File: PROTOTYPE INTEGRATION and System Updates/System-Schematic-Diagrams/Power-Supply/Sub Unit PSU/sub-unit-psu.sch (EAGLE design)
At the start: 8 parts, among them U1 BA033CC0FP-E2TO252-3_ROM, U3 L7805CV

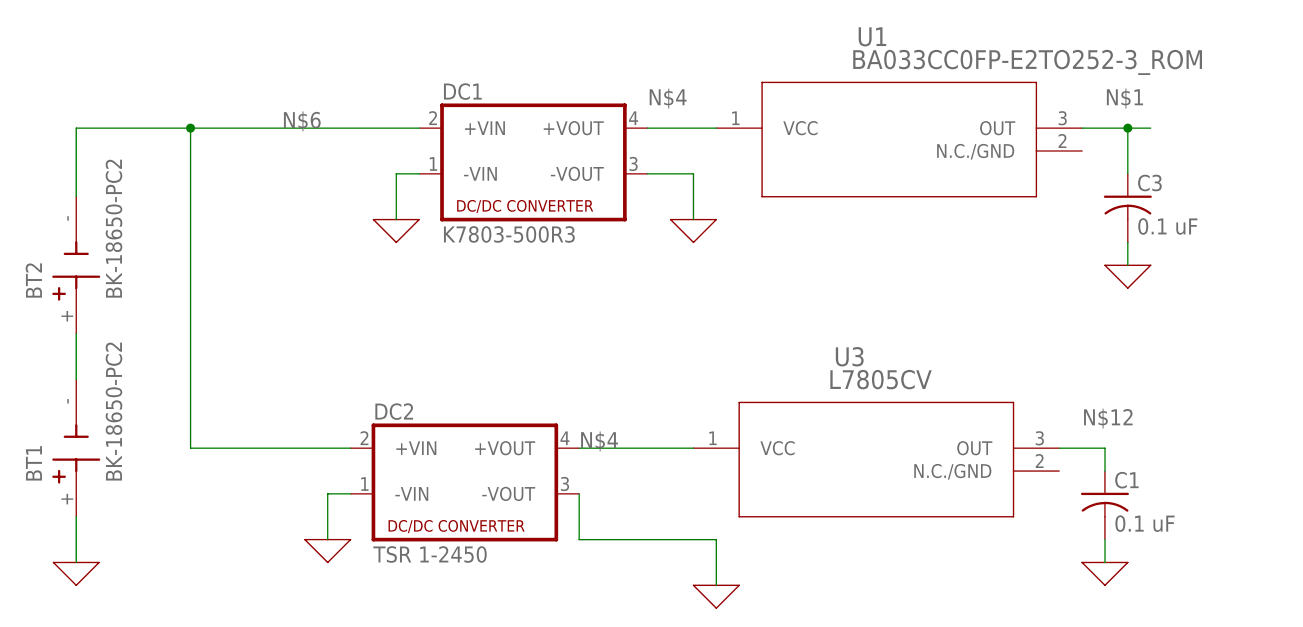
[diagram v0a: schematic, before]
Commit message: Updated Individual schematics, bd and pictures
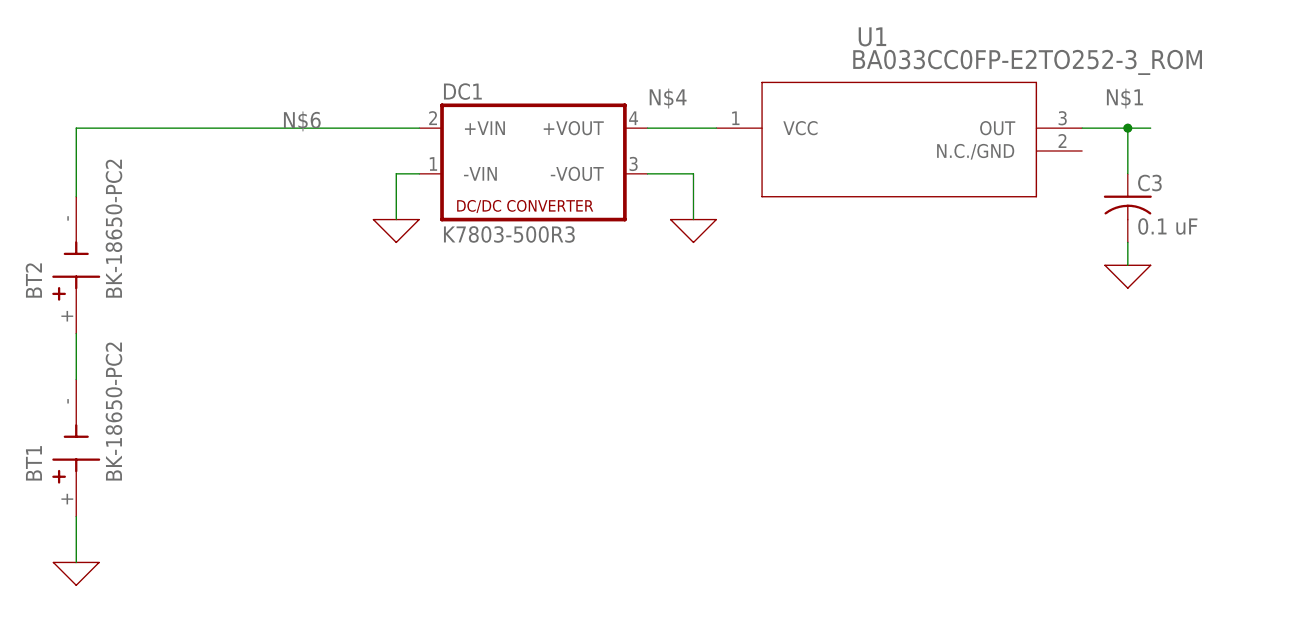
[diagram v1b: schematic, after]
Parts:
- removed C1: 0.1 uF, rcl:C-US050-024X044
- removed DC2: TSR 1-2450, dc-dc-converter:NME
- removed U3: L7805CV, 2023-03-08_12-17-23_Library:BA033CC0FP-E2TO252-3_ROM
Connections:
- removed net N$12: C1.1, U3.OUT
- net 0: no longer C1.2, DC2.-VIN, DC2.-VOUT
- net N$4: no longer DC2.+VOUT, U3.VCC
- net N$6: no longer DC2.+VIN
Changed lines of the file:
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@@
 <part name="C3" library="rcl" library_urn="urn:adsk.eagle:library:334" deviceset="C-US" device="050-024X044" package3d_urn="urn:adsk.eagle:package:23643/1" value="0.1 uF"/>
 <part name="X_10" library="ngspice-simulation" library_urn="urn:adsk.eagle:library:527439" deviceset="GND" device=""/>
-<part name="DC2" library="dc-dc-converter" library_urn="urn:adsk.eagle:library:208" deviceset="NME" device="" package3d_urn="urn:adsk.eagle:package:12313/1" value="TSR 1-2450"/>
-<part name="X_6" library="ngspice-simulation" library_urn="urn:adsk.eagle:library:527439" deviceset="GND" device=""/>
-<part name="U3" library="2023-03-08_12-17-23_Library" deviceset="BA033CC0FP-E2" device="TO252-3_ROM" value="L7805CV"/>
-<part name="X_8" library="ngspice-simulation" library_urn="urn:adsk.eagle:library:527439" deviceset="GND" device=""/>
-<part name="C1" library="rcl" library_urn="urn:adsk.eagle:library:334" deviceset="C-US" device="050-024X044" package3d_urn="urn:adsk.eagle:package:23643/1" value="0.1 uF"/>
-<part name="X_3" library="ngspice-simulation" library_urn="urn:adsk.eagle:library:527439" deviceset="GND" device=""/>
 </parts>
 <sheets>
@@
 </instance>
 <instance part="X_10" gate="G$1" x="233.68" y="134.62" smashed="yes"/>
-<instance part="DC2" gate="G$1" x="160.02" y="111.76" smashed="yes">
-<attribute name="NAME" x="149.86" y="117.475" size="1.778" layer="95"/>
-<attribute name="VALUE" x="149.86" y="101.6" size="1.778" layer="96"/>
-</instance>
-<instance part="X_6" gate="G$1" x="144.78" y="104.14" smashed="yes"/>
-<instance part="U3" gate="A" x="182.88" y="114.3" smashed="yes">
-<attribute name="NAME" x="201.0146" y="123.4186" size="2.083" layer="95" ratio="6"/>
-<attribute name="VALUE" x="200.3752" y="120.8786" size="2.083" layer="96" ratio="6"/>
-</instance>
-<instance part="X_8" gate="G$1" x="187.96" y="99.06" smashed="yes"/>
-<instance part="C1" gate="G$1" x="231.14" y="109.22" smashed="yes">
-<attribute name="NAME" x="232.156" y="109.855" size="1.778" layer="95"/>
-<attribute name="VALUE" x="232.156" y="105.029" size="1.778" layer="96"/>
-</instance>
-<instance part="X_3" gate="G$1" x="231.14" y="101.6" smashed="yes"/>
 </instances>
 <busses>
@@
 <wire x1="233.68" y1="134.62" x2="233.68" y2="137.16" width="0.1524" layer="91"/>
 </segment>
-<segment>
-<pinref part="X_6" gate="G$1" pin="0"/>
-<pinref part="DC2" gate="G$1" pin="-VIN"/>
-<wire x1="144.78" y1="104.14" x2="144.78" y2="109.22" width="0.1524" layer="91"/>
-<wire x1="144.78" y1="109.22" x2="147.32" y2="109.22" width="0.1524" layer="91"/>
-</segment>
-<segment>
-<pinref part="DC2" gate="G$1" pin="-VOUT"/>
-<wire x1="172.72" y1="109.22" x2="172.72" y2="104.14" width="0.1524" layer="91"/>
-<wire x1="172.72" y1="104.14" x2="187.96" y2="104.14" width="0.1524" layer="91"/>
-<pinref part="X_8" gate="G$1" pin="0"/>
-<wire x1="187.96" y1="99.06" x2="187.96" y2="104.14" width="0.1524" layer="91"/>
-</segment>
-<segment>
-<pinref part="X_3" gate="G$1" pin="0"/>
-<pinref part="C1" gate="G$1" pin="2"/>
-<wire x1="231.14" y1="101.6" x2="231.14" y2="104.14" width="0.1524" layer="91"/>
-</segment>
 </net>
 <net name="N$4" class="0">
@@
 <label x="180.34" y="152.4" size="1.778" layer="95"/>
 <pinref part="U1" gate="A" pin="VCC"/>
-</segment>
-<segment>
-<pinref part="DC2" gate="G$1" pin="+VOUT"/>
-<wire x1="172.72" y1="114.3" x2="185.42" y2="114.3" width="0.1524" layer="91"/>
-<label x="172.72" y="114.3" size="1.778" layer="95"/>
-<pinref part="U3" gate="A" pin="VCC"/>
 </segment>
 </net>
@@
 </segment>
 </net>
-<net name="N$12" class="0">
+<net name="N$6" class="0">
 <segment>
-<wire x1="226.06" y1="114.3" x2="231.14" y2="114.3" width="0.1524" layer="91"/>
-<label x="228.6" y="116.84" size="1.778" layer="95"/>
-<pinref part="U3" gate="A" pin="OUT"/>
-<pinref part="C1" gate="G$1" pin="1"/>
-<wire x1="231.14" y1="111.76" x2="231.14" y2="114.3" width="0.1524" layer="91"/>
+<pinref part="DC1" gate="G$1" pin="+VIN"/>
+<label x="139.7" y="149.86" size="1.778" layer="95"/>
+<pinref part="BT2" gate="G$1" pin="-"/>
+<wire x1="116.84" y1="149.86" x2="154.94" y2="149.86" width="0.1524" layer="91"/>
+<wire x1="116.84" y1="142.24" x2="116.84" y2="149.86" width="0.1524" layer="91"/>
 </segment>
 </net>
-<net name="N$6" class="0">
-<segment>
-<pinref part="DC2" gate="G$1" pin="+VIN"/>
-<wire x1="129.54" y1="114.3" x2="147.32" y2="114.3" width="0.1524" layer="91"/>
-<pinref part="DC1" gate="G$1" pin="+VIN"/>
-<wire x1="116.84" y1="149.86" x2="129.54" y2="149.86" width="0.1524" layer="91"/>
-<label x="139.7" y="149.86" size="1.778" layer="95"/>
-<pinref part="BT2" gate="G$1" pin="-"/>
-<wire x1="129.54" y1="149.86" x2="154.94" y2="149.86" width="0.1524" layer="91"/>
-<wire x1="116.84" y1="142.24" x2="116.84" y2="149.86" width="0.1524" layer="91"/>
-<wire x1="129.54" y1="114.3" x2="129.54" y2="149.86" width="0.1524" layer="91"/>
-<junction x="129.54" y="149.86"/>
-</segment>
-</net>
